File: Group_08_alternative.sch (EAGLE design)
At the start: 29 parts, among them J1 POWER_JACKPTH_LOCK, U1 +12v, U3 TCA9546ATSSOP, U4 TMUX1208

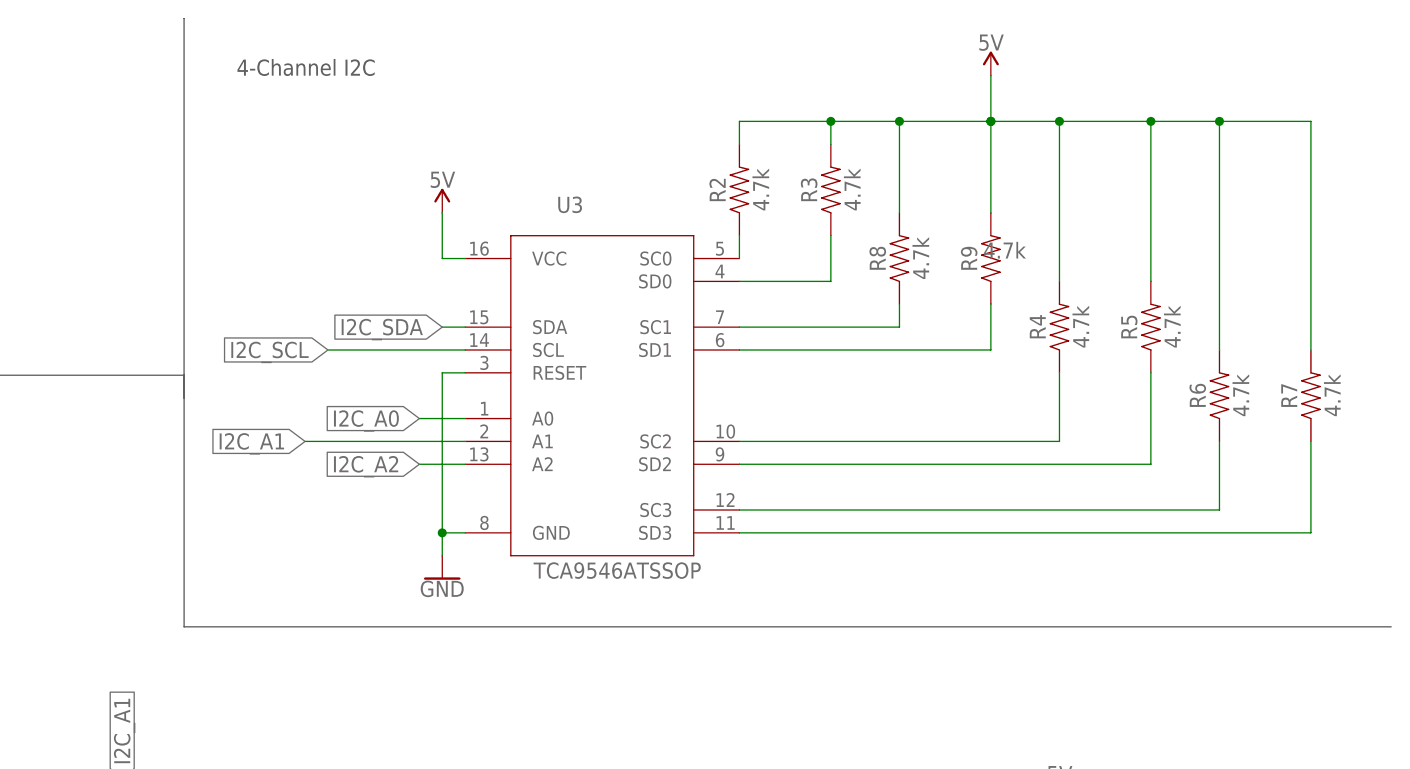
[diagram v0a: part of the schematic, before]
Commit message: Optimized board, added silkscreen. 0 errors after performing DCR.
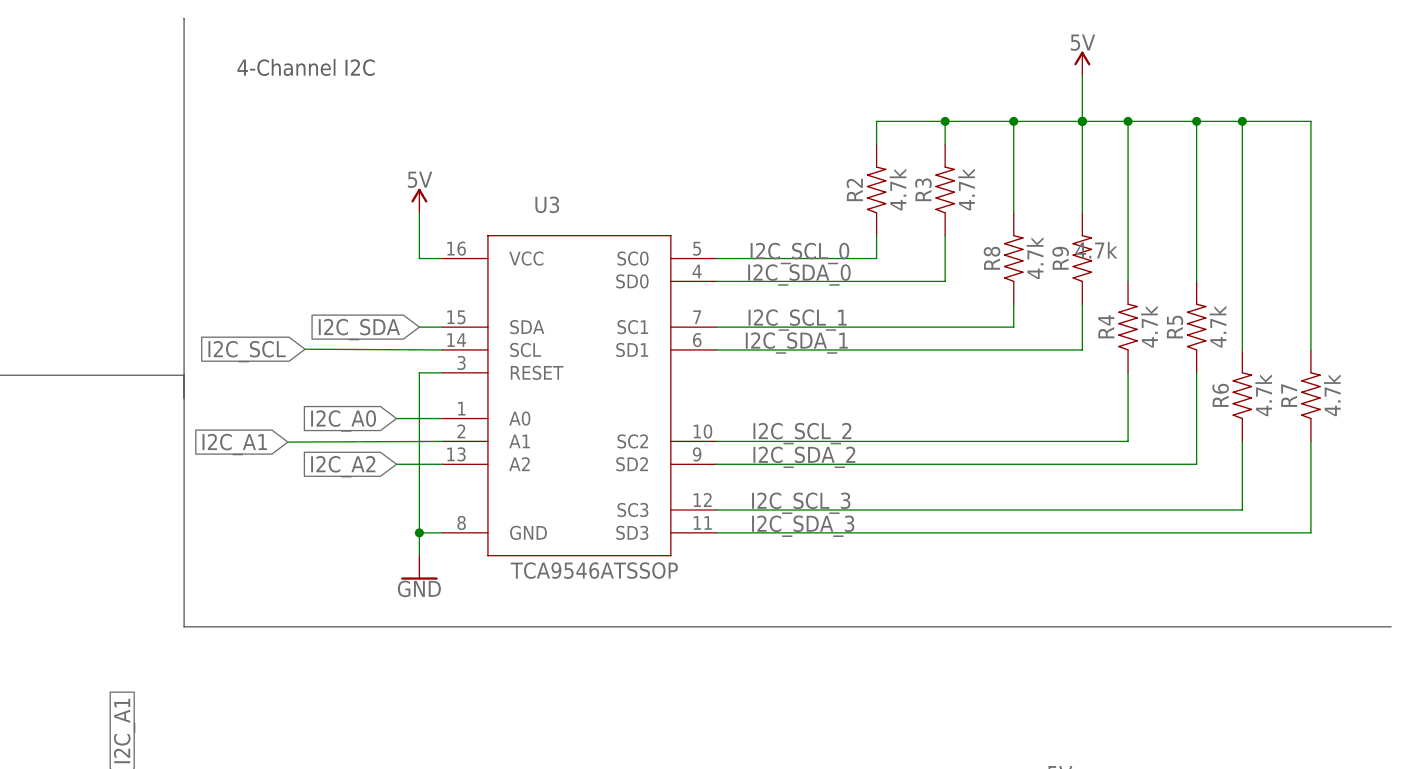
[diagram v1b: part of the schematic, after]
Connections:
- removed net N$1: R2.1, U3.SC0
- removed net N$3: R3.1, U3.SD0
- removed net N$4: R8.1, U3.SC1
- removed net N$5: R9.1, U3.SD1
- removed net N$6: R4.1, U3.SC2
- removed net N$7: R5.1, U3.SD2
- removed net N$8: R6.1, U3.SC3
- removed net N$9: R7.1, U3.SD3
- net I2C_SCL_0: now also R2.1, U3.SC0
- net I2C_SCL_1: now also R8.1, U3.SC1
- net I2C_SCL_2: now also R4.1, U3.SC2
- net I2C_SCL_3: now also R6.1, U3.SC3
- net I2C_SDA_0: now also R3.1, U3.SD0
- net I2C_SDA_1: now also R9.1, U3.SD1
- net I2C_SDA_2: now also R5.1, U3.SD2
- net I2C_SDA_3: now also R7.1, U3.SD3
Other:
- moved on the sheet: R2, R3, R4, R5, R6, R8, R9, U3
